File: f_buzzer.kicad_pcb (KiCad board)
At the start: 2 copper layers, 71.5 x 44 mm, 0 parts

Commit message: Rev1
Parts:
- added BZ1: Buzzer, Buzzer_Beeper:Buzzer_15x7.5RM7.6, F.Cu at (165.2, 86.2)
- added C1: C, Capacitor_THT:C_Disc_D5.1mm_W3.2mm_P5.00mm, F.Cu at (127.6, 79.9)
- added C2: C, Capacitor_THT:C_Disc_D5.1mm_W3.2mm_P5.00mm, F.Cu at (148.5, 88.2)
- added C3: C, Capacitor_THT:C_Disc_D5.1mm_W3.2mm_P5.00mm, F.Cu at (160.7, 105.5)
- added R1: 330, Resistor_THT:R_Axial_DIN0207_L6.3mm_D2.5mm_P7.62mm_Horizontal, F.Cu at (153.1, 101.2)
- added R2: 27K, Resistor_THT:R_Axial_DIN0207_L6.3mm_D2.5mm_P7.62mm_Horizontal, F.Cu at (137.1, 100.1)
- added R3: 27K, Resistor_THT:R_Axial_DIN0207_L6.3mm_D2.5mm_P7.62mm_Horizontal, F.Cu at (150.3, 80.9)
- added REF**: PinHeader_1x03_P2.54mm_Horizontal, f_buzzer:PinHeader_1x03_P2.54mm_Horizontal, F.Cu at (181.6, 86.2)
- added RV1: 20K, f_buzzer:Potentiometer_Bourns_3345P_Horizontal, F.Cu at (128.5, 108.4)
- added U1: SN74123N, Package_DIP:DIP-16_W7.62mm, F.Cu at (139.1, 86.9)
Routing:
- net GND: track 0.00 -> 128.9 mm
- net Net-(BZ1-Pad1): track 0.00 -> 91.9 mm
- net VCC: track 0.00 -> 64.6 mm
- net /DVR: track 0.00 -> 63.3 mm
- net Net-(BZ1-Pad2): track 0.00 -> 54.9 mm
- net Net-(R1-Pad1): track 0.00 -> 44.9 mm
- net Net-(C3-Pad1): track 0.00 -> 34.6 mm
- net Net-(C1-Pad2): track 0.00 -> 30.0 mm
- net Net-(C2-Pad1): track 0.00 -> 24.1 mm
- net Net-(C2-Pad2): track 0.00 -> 12.7 mm
- net Net-(U1-Pad10): track 0.00 -> 11.1 mm
- net Net-(C1-Pad1): track 0.00 -> 7.46 mm
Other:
- outline, holes or cut-outs redrawn

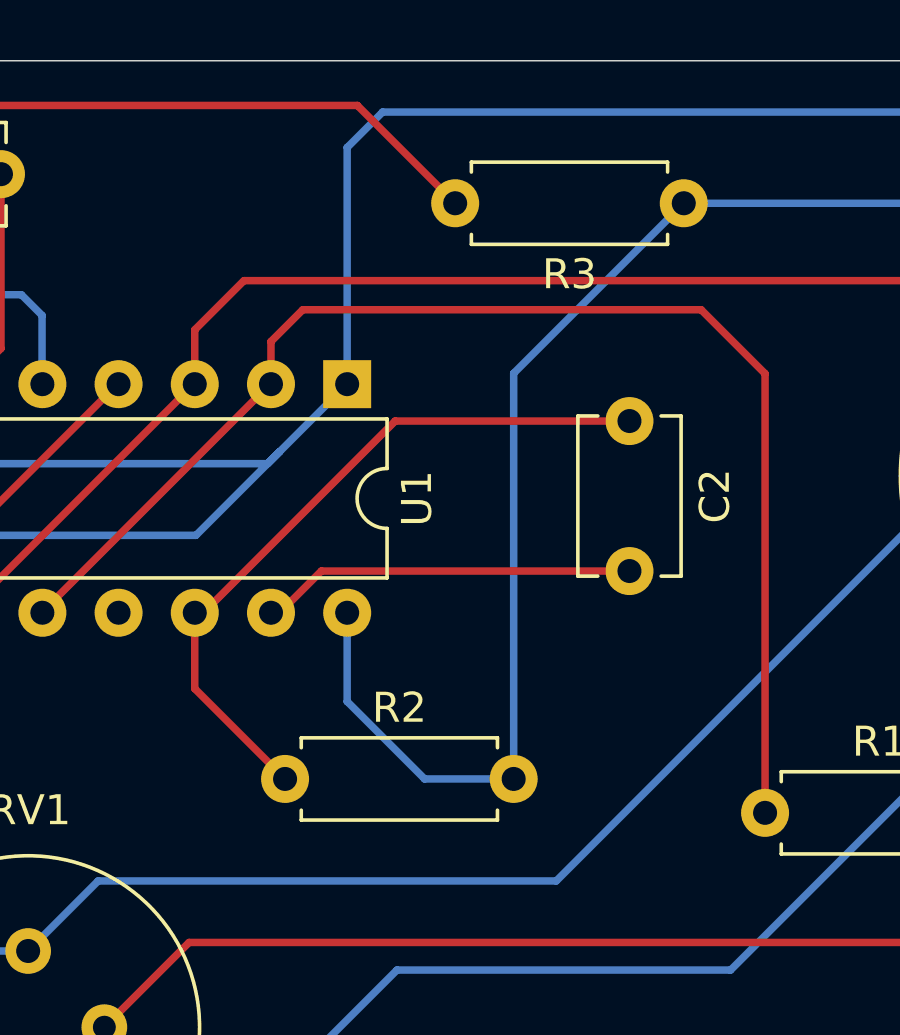
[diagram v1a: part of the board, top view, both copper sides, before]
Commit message: Fixed connections in schematic
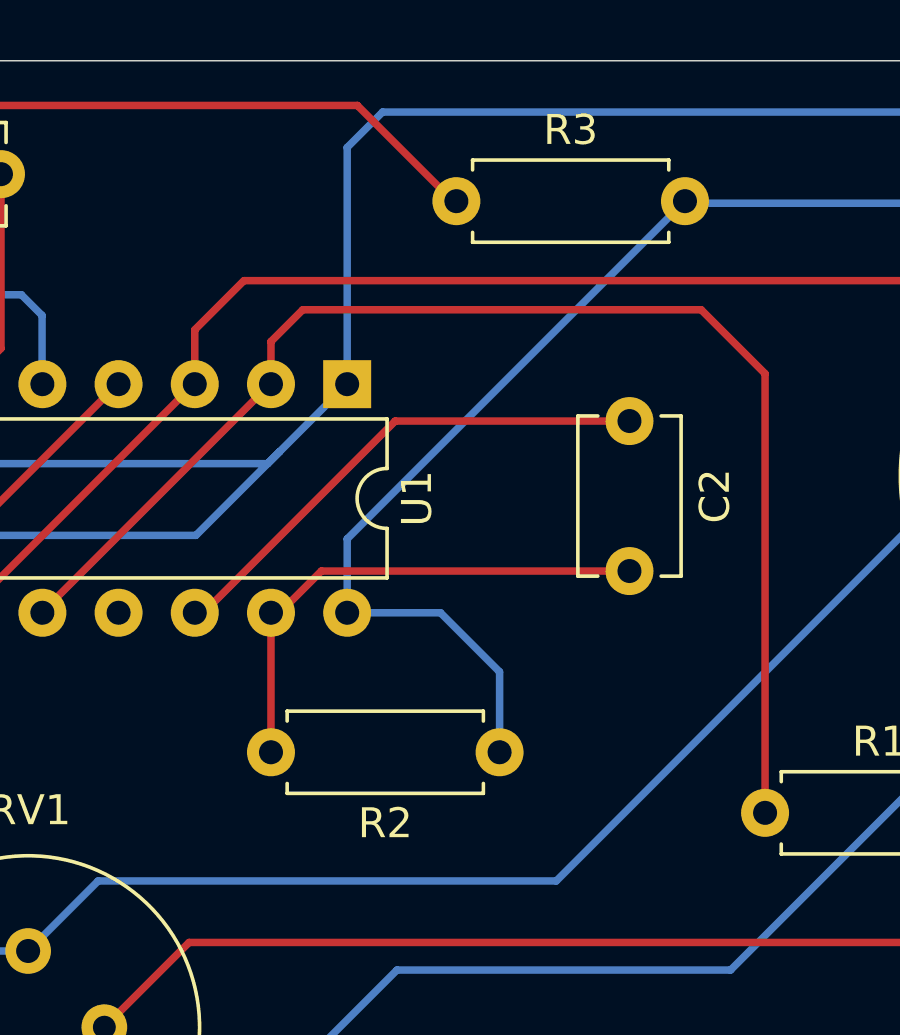
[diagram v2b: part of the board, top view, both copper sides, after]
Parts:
- C1, C2: value C -> 20n
- moved R3 7.58 mm to (142.8, 80.8), turned to 0 degrees
- moved R2 7.21 mm to (144.2, 99.2), turned to 180 degrees
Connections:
- R2 pad 1: Net-(C2-Pad1) -> VCC
- R2 pad 2: VCC -> Net-(C2-Pad2)
- R3 pad 1: VCC -> Net-(C1-Pad2)
- R3 pad 2: Net-(C1-Pad2) -> VCC
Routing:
- net Net-(C2-Pad1): track 24.1 -> 17.3 mm
- net Net-(C2-Pad2): track 12.7 -> 17.3 mm
- net VCC: track 64.6 -> 60.4 mm

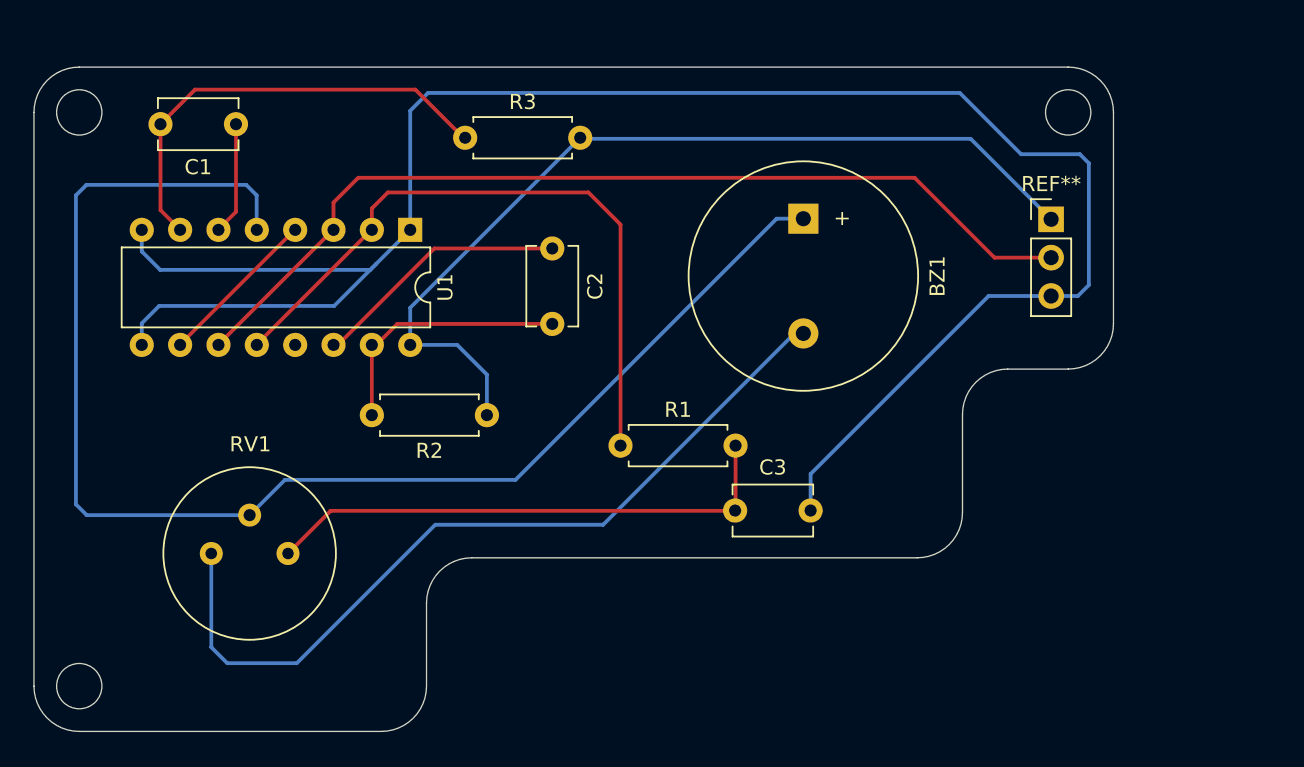
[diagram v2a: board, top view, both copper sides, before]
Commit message: Added some constraints related to the case
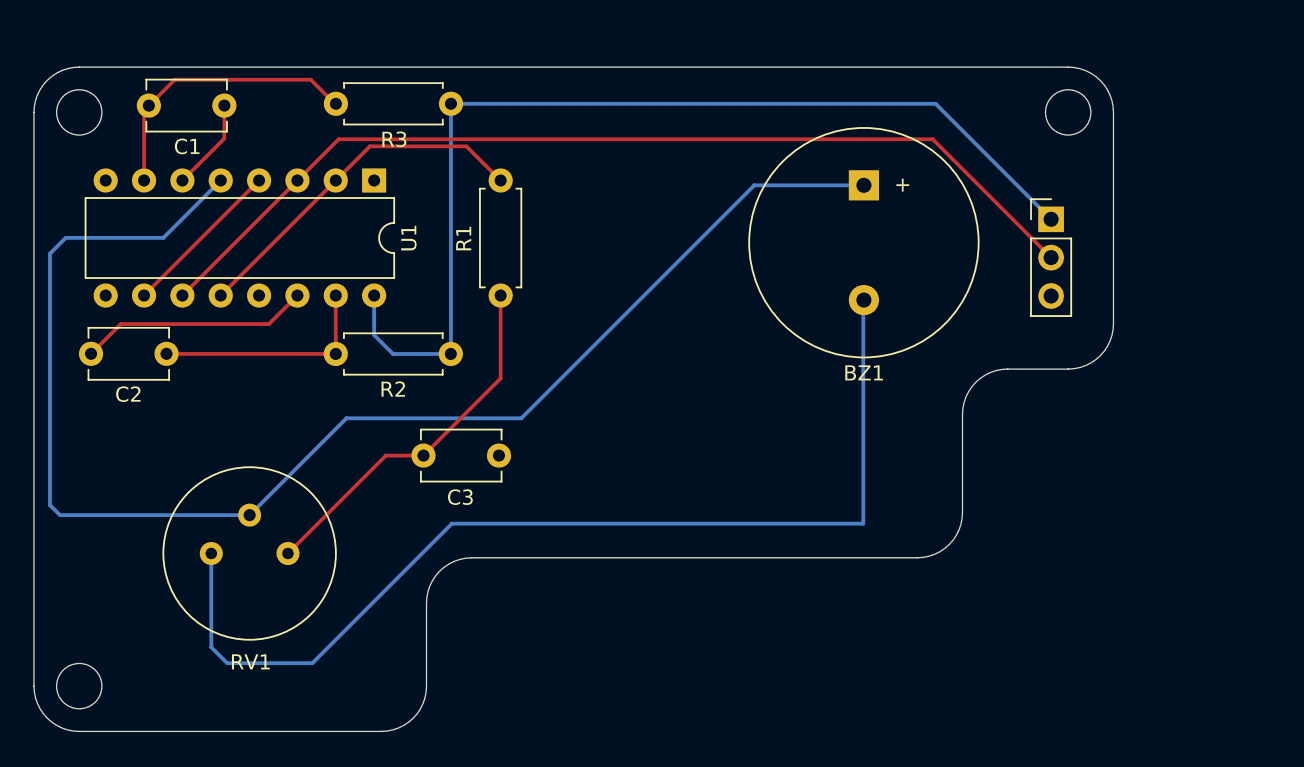
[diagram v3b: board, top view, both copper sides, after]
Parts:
- moved C2 31.3 mm to (118.0, 95.1), turned to 0 degrees
- moved C3 21.0 mm to (140.0, 101.9)
- moved R1 19.3 mm to (145.1, 83.7), turned to 270 degrees
- moved R3 8.85 mm to (134.2, 78.6)
- moved R2 4.70 mm to (141.8, 95.2)
- moved BZ1 4.58 mm to (169.2, 84.0)
- moved U1 4.05 mm to (136.7, 83.7)
- moved C1 1.45 mm to (126.8, 78.7)
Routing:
- net GND: track 128.9 -> 0.00 mm
- net Net-(R1-Pad1): track 44.9 -> 23.6 mm
- net Net-(BZ1-Pad2): track 54.9 -> 68.3 mm
- net Net-(C1-Pad2): track 30.0 -> 18.8 mm
- net Net-(C3-Pad1): track 34.6 -> 24.4 mm
- net VCC: track 60.4 -> 67.7 mm
- net Net-(C2-Pad2): track 17.3 -> 15.1 mm
- net Net-(C2-Pad1): track 17.3 -> 15.3 mm
- net /DVR: track 63.3 -> 65.1 mm
- net Net-(C1-Pad1): track 7.46 -> 6.11 mm
- net Net-(BZ1-Pad1): track 91.9 -> 93.2 mm
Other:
- board text added: "DVR"
- board text added: "GND"
- board text added: "No components should be located inside the circle (except for the potentiometer). The surface of the disc is visible from the cutout of the back case of the IBM 4704 series keyboard."
- board text added: "No components should be placed inside the cercle. This where the IBM 4704 series keyboard feet attaches to the back case."
- board text added: "These areas are to be avoided for placing components or pads."
- board text added: "This is the area where the buzzer could fit on the top of the board."
- board text added: "VCC"

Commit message: Replaced the buzzer with the 22mm generic one
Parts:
- BZ1: footprint Buzzer_Beeper:Buzzer_15x7.5RM7.6 -> f_buzzer:buzzer_front
- moved BZ1 4.40 mm to (168.8, 88.4), turned to 0 degrees
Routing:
- net Net-(BZ1-Pad2): track 68.3 -> 58.7 mm
- net /DVR: track 65.1 -> 68.3 mm
- net VCC: track 67.7 -> 69.4 mm
- net Net-(BZ1-Pad1): track 93.2 -> 93.8 mm
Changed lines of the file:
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@@
   (general
     (thickness 1.6)
-    (drawings 49)
-    (tracks 50)
+    (drawings 48)
+    (tracks 51)
     (zones 0)
     (modules 10)
@@
     (add_net VCC)
   )
-  (module Buzzer_Beeper:Buzzer_15x7.5RM7.6 (layer F.Cu)
-    (at 169.18 83.98 270)
-    (descr "Generic Buzzer, D15mm height 7.5mm with RM7.6mm")
-    (tags buzzer)
-    (fp_text reference BZ1 (at 12.46 -0.01) (layer F.SilkS)
-      (effects (font (size 1 1) (thickness 0.15)))
-    )
-    (fp_text value Buzzer (at 3.81 8.89 90) (layer F.Fab)
-      (effects (font (size 1 1) (thickness 0.15)))
-    )
-    (fp_text user %R (at 3.8 -4 90) (layer F.Fab)
-      (effects (font (size 1 1) (thickness 0.15)))
-    )
-    (fp_text user + (at -0.01 -2.54 90) (layer F.SilkS)
-      (effects (font (size 1 1) (thickness 0.15)))
-    )
-    (fp_text user + (at -0.01 -2.54 90) (layer F.Fab)
-      (effects (font (size 1 1) (thickness 0.15)))
-    )
-    (fp_circle (center 3.8 0) (end 11.55 0) (layer F.CrtYd) (width 0.05))
-    (fp_circle (center 3.8 0) (end 11.3 0) (layer F.Fab) (width 0.1))
-    (fp_circle (center 3.8 0) (end 4.8 0) (layer F.Fab) (width 0.1))
-    (fp_circle (center 3.8 0) (end 11.4 0) (layer F.SilkS) (width 0.12))
-    (pad 2 thru_hole circle (at 7.6 0 270) (size 2 2) (drill 1) (layers *.Cu *.Mask)
+  (module f_buzzer:buzzer_front (layer F.Cu)
+    (at 168.81 88.36)
+    (fp_text reference BZ1 (at -0.02 -12.32) (layer F.SilkS) hide
+      (effects (font (size 1 1) (thickness 0.15)))
+    )
+    (fp_text value Buzzer (at -0.02 12.22) (layer F.Fab)
+      (effects (font (size 1 1) (thickness 0.15)))
+    )
+    (fp_circle (center 0 0) (end 8.59 6.68) (layer F.Fab) (width 0.12))
+    (fp_circle (center 0 0) (end 11 0) (layer F.SilkS) (width 0.12))
+    (pad 1 thru_hole oval (at 0 -5.87) (size 1 10) (drill oval 0.7 9.7) (layers *.Cu *.Mask)
+      (net 2 "Net-(BZ1-Pad1)"))
+    (pad 2 thru_hole oval (at -0.01 5.87) (size 1 10) (drill oval 0.7 9.7) (layers *.Cu *.Mask)
       (net 1 "Net-(BZ1-Pad2)"))
-    (pad 1 thru_hole rect (at 0 0 270) (size 2 2) (drill 1) (layers *.Cu *.Mask)
-      (net 2 "Net-(BZ1-Pad1)"))
-    (model ${KISYS3DMOD}/Buzzer_Beeper.3dshapes/Buzzer_15x7.5RM7.6.wrl
-      (at (xyz 0 0 0))
-      (scale (xyz 1 1 1))
-      (rotate (xyz 0 0 0))
-    )
   )
   (module Package_DIP:DIP-16_W7.62mm (layer F.Cu)
@@
     )
   )
-  (gr_circle (center 168.97 87.87) (end 179.97 87.87) (layer Dwgs.User) (width 0.12))
   (gr_text "These areas are to be avoided for placing components or pads." (at 143.64 66.34) (layer Cmts.User)
     (effects (font (size 1 1) (thickness 0.15)))
@@
   (gr_line (start 182.71 76.15) (end 117.21 76.15) (layer Edge.Cuts) (width 0.05))
   (gr_line (start 114.21 117.15) (end 114.21 79.15) (layer Edge.Cuts) (width 0.05))
+  (segment (start 127.01 115.63) (end 125.955 114.575) (width 0.25) (layer B.Cu) (net 1))
   (segment (start 132.65 115.63) (end 127.01 115.63) (width 0.25) (layer B.Cu) (net 1))
-  (segment (start 169.14 106.39) (end 141.89 106.39) (width 0.25) (layer B.Cu) (net 1))
   (segment (start 125.955 114.575) (end 125.955 108.365) (width 0.25) (layer B.Cu) (net 1))
+  (segment (start 156.31 106.39) (end 141.89 106.39) (width 0.25) (layer B.Cu) (net 1))
   (segment (start 141.89 106.39) (end 132.65 115.63) (width 0.25) (layer B.Cu) (net 1))
-  (segment (start 127.01 115.63) (end 125.955 114.575) (width 0.25) (layer B.Cu) (net 1))
-  (segment (start 169.14 91.71) (end 169.14 106.39) (width 0.25) (layer B.Cu) (net 1))
+  (segment (start 168.96 93.74) (end 156.31 106.39) (width 0.25) (layer B.Cu) (net 1))
   (segment (start 116.32 87.46) (end 122.78 87.46) (width 0.25) (layer B.Cu) (net 2))
   (segment (start 115.27 88.51) (end 116.32 87.46) (width 0.25) (layer B.Cu) (net 2))
@@
   (segment (start 128.495 105.825) (end 115.935 105.825) (width 0.25) (layer B.Cu) (net 2))
   (segment (start 134.91 99.41) (end 128.495 105.825) (width 0.25) (layer B.Cu) (net 2))
-  (segment (start 161.92 83.98) (end 146.49 99.41) (width 0.25) (layer B.Cu) (net 2))
   (segment (start 146.49 99.41) (end 134.91 99.41) (width 0.25) (layer B.Cu) (net 2))
-  (segment (start 169.18 83.98) (end 161.92 83.98) (width 0.25) (layer B.Cu) (net 2))
+  (segment (start 163.9 82) (end 146.49 99.41) (width 0.25) (layer B.Cu) (net 2))
+  (segment (start 168.97 82) (end 163.9 82) (width 0.25) (layer B.Cu) (net 2))
   (segment (start 121.5 79.02) (end 121.5 83.66) (width 0.25) (layer F.Cu) (net 3))
   (segment (start 121.82 78.7) (end 121.5 79.02) (width 0.25) (layer F.Cu) (net 3))
@@
   (segment (start 136.74 93.9) (end 137.99 95.15) (width 0.25) (layer B.Cu) (net 10))
   (segment (start 136.74 91.28) (end 136.74 93.9) (width 0.25) (layer B.Cu) (net 10))
-  (segment (start 181.58 86.23) (end 173.93 78.58) (width 0.25) (layer B.Cu) (net 10))
-  (segment (start 173.93 78.58) (end 141.83 78.58) (width 0.25) (layer B.Cu) (net 10))
+  (segment (start 143.86 76.55) (end 141.83 78.58) (width 0.25) (layer B.Cu) (net 10))
+  (segment (start 171.9 76.55) (end 143.86 76.55) (width 0.25) (layer B.Cu) (net 10))
+  (segment (start 181.58 86.23) (end 171.9 76.55) (width 0.25) (layer B.Cu) (net 10))
   (segment (start 131.66 83.66) (end 124.04 91.28) (width 0.25) (layer F.Cu) (net 12))
-  (segment (start 181.58 88.77) (end 173.74 80.93) (width 0.25) (layer F.Cu) (net 12))
-  (segment (start 173.74 80.93) (end 134.39 80.93) (width 0.25) (layer F.Cu) (net 12))
-  (segment (start 134.39 80.93) (end 131.66 83.66) (width 0.25) (layer F.Cu) (net 12))
+  (segment (start 138.28 77.04) (end 131.66 83.66) (width 0.25) (layer F.Cu) (net 12))
+  (segment (start 169.85 77.04) (end 138.28 77.04) (width 0.25) (layer F.Cu) (net 12))
+  (segment (start 181.58 88.77) (end 169.85 77.04) (width 0.25) (layer F.Cu) (net 12))
   (segment (start 129.12 83.66) (end 121.5 91.28) (width 0.25) (layer F.Cu) (net 13))
 )
